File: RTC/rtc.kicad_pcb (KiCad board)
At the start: 2 copper layers, 8 parts, among them P1 CONN_01X04, P2 CONN_01X01, U1 MCP7940N, U2 32.768kHz

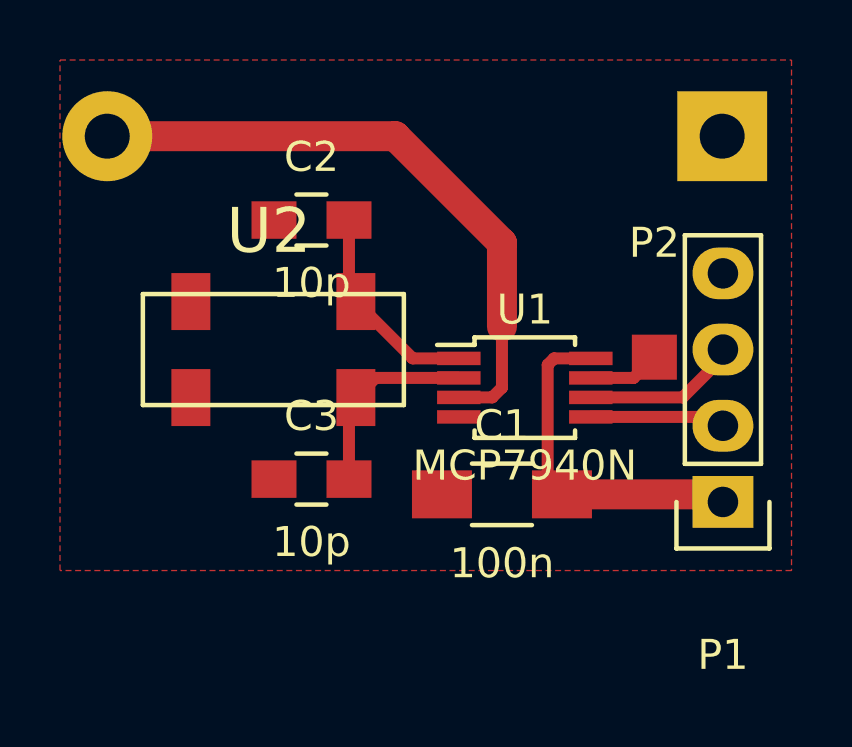
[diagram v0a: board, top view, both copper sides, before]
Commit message: some bugs at rtc fixed
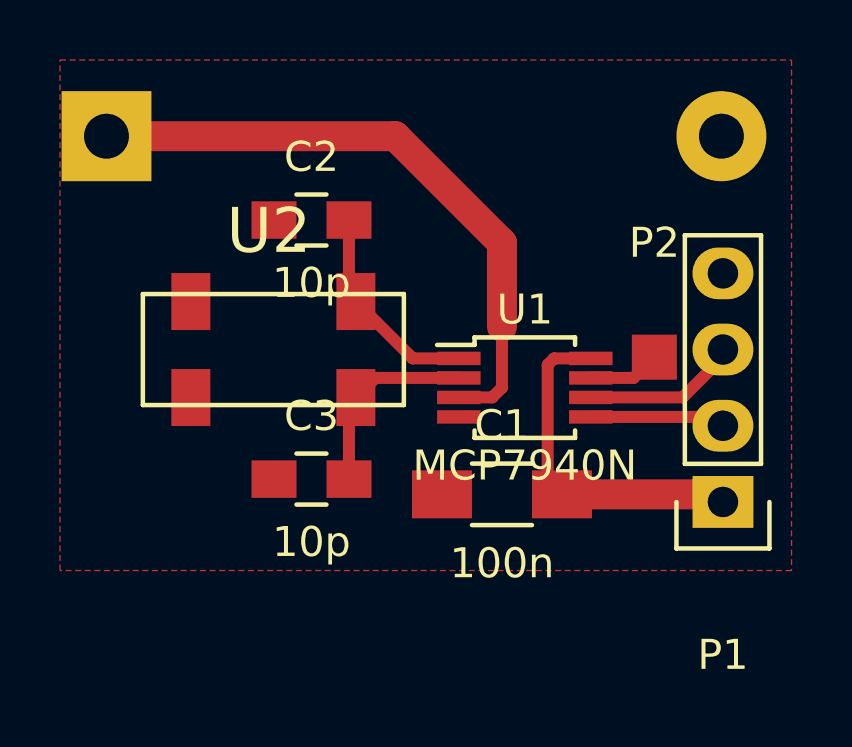
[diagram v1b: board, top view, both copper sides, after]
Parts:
- moved BT1 9.91 mm to (162.1, 98.3), turned to 180 degrees
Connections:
- BT1 pad 1: GND -> Net-(BT1-Pad1)
- BT1 pad 2: Net-(BT1-Pad2) -> GND
- U1 pad 3: Net-(BT1-Pad2) -> Net-(BT1-Pad1)
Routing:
- net Net-(BT1-Pad2): track 21.0 -> 0.00 mm
- net Net-(BT1-Pad1): track 0.00 -> 21.0 mm
